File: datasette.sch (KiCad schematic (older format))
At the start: 30 parts, among them CN3 CASSETTE, CN7 SERIAL_BUS, Q5 2SD880, U11 74LS125, U9 74LS06

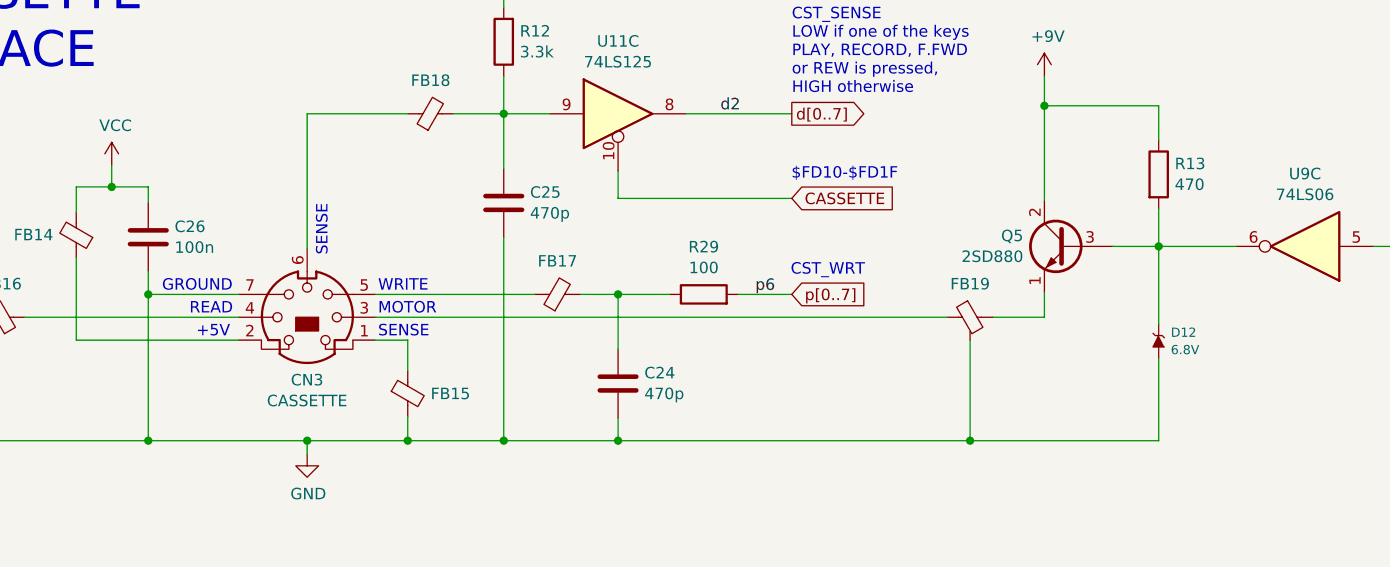
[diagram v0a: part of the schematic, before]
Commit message: Add support for PLA16V8
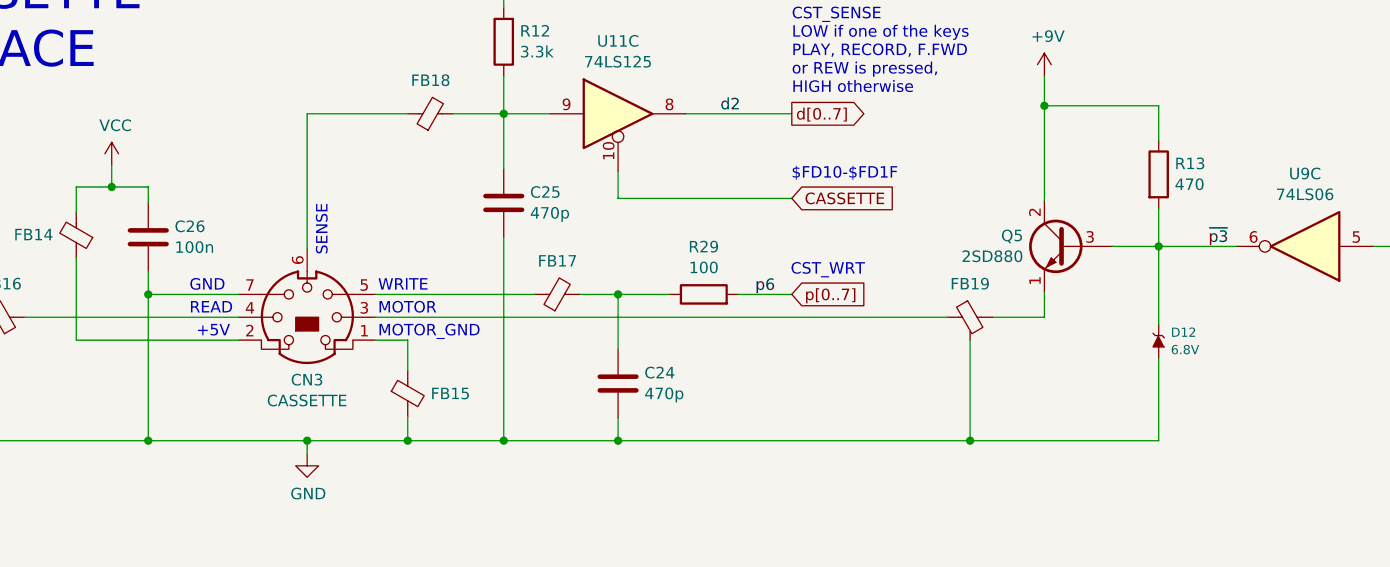
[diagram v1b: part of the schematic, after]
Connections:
- net ~p3: now reaches D12.2 (K), Q5.3 (B), R13.2, U9.6
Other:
- note added: "MOTOR_GND"
- note removed: "GROUND"
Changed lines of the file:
@@
 MOTOR
 Text Notes 5350 2560 0    50   ~ 0
-SENSE
-Text Notes 4405 2360 0    50   ~ 0
-GROUND
+MOTOR_GND
+Text Notes 4525 2360 0    50   ~ 0
+GND
 Text Notes 4525 2460 0    50   ~ 0
 READ
@@
 Wire Bus Line
 	3565 4640 3565 5520
+Text Label 9070 2155 2    50   ~ 0
+~p3
 $EndSCHEMATC

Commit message: Switch to Kycon MiniDIN connectors
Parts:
- removed CN3: CASSETTE, LittleSixteen:Connector_Mini-DIN_Female_7Pin_2rows, symbol Connector:Mini-DIN-7
- added CN3: CASSETTE, LittleSixteen:KMDGX-7S-BS, symbol mini-din-7:Mini-DIN-7
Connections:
- net GND: now also CN3.0 (SH), CN3.8
- net at FB19.1: now also CN3.3
- net at FB15.1: now also CN3.1
- net at FB14.1: now also CN3.2
- net at FB16.1: now also CN3.5
- net at FB17.1: now also CN3.6
- net at FB18.1: now also CN3.7
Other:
- note added: "WARNING: The drawing of\nthis connector does not\nmatch the real connector\nexactly!"
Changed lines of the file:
@@
 Sheet 7 12
 Title "LittleSixteen"
-Date "2021-10-31"
+Date "2021-11-06"
 Rev "2git"
 Comp "SukkoPera"
@@
 Comment4 ""
 $EndDescr
-$Comp
-L Connector:Mini-DIN-7 CN3
-U 1 1 5ECB4902
-P 5040 2465
-F 0 "CN3" H 5040 2190 50  0000 C CNN
-F 1 "CASSETTE" H 5040 2099 50  0000 C CNN
-F 2 "LittleSixteen:Connector_Mini-DIN_Female_7Pin_2rows" V 5030 2455 50  0001 C CNN
-F 3 "http://service.powerdynamics.com/ec/Catalog17/Section%2011.pdf" V 5030 2455 50  0001 C CNN
-	1    5040 2465
-	1    0    0    -1
-$EndComp
 Wire Wire Line
 	4740 2365 4345 2365
@@
 Text Notes 3495 4505 2    50   ~ 0
 These are more retrofitted\nprotection diodes, these\nare present on most C16s\nI've seen; note that these\ndiodes have been added on all\npins going straight to the CPU
+Text Label 9070 2155 2    50   ~ 0
+~p3
+$Comp
+L mini-din-7:Mini-DIN-7 CN3
+U 1 1 620EE6EF
+P 5040 2465
+F 0 "CN3" H 4845 2215 50  0000 C CNN
+F 1 "CASSETTE" H 4745 2130 50  0000 C CNN
+F 2 "LittleSixteen:KMDGX-7S-BS" V 5030 2455 50  0001 C CNN
+F 3 "http://service.powerdynamics.com/ec/Catalog17/Section%2011.pdf" V 5030 2455 50  0001 C CNN
+	1    5040 2465
+	1    0    0    -1
+$EndComp
+Text Notes 4995 2155 1    50   ~ 0
+WARNING: The drawing of\nthis connector does not\nmatch the real connector\nexactly!
+Wire Wire Line
+	5040 2765 5040 3005
 Wire Bus Line
 	3565 4640 3565 5520
-Text Label 9070 2155 2    50   ~ 0
-~p3
 $EndSCHEMATC

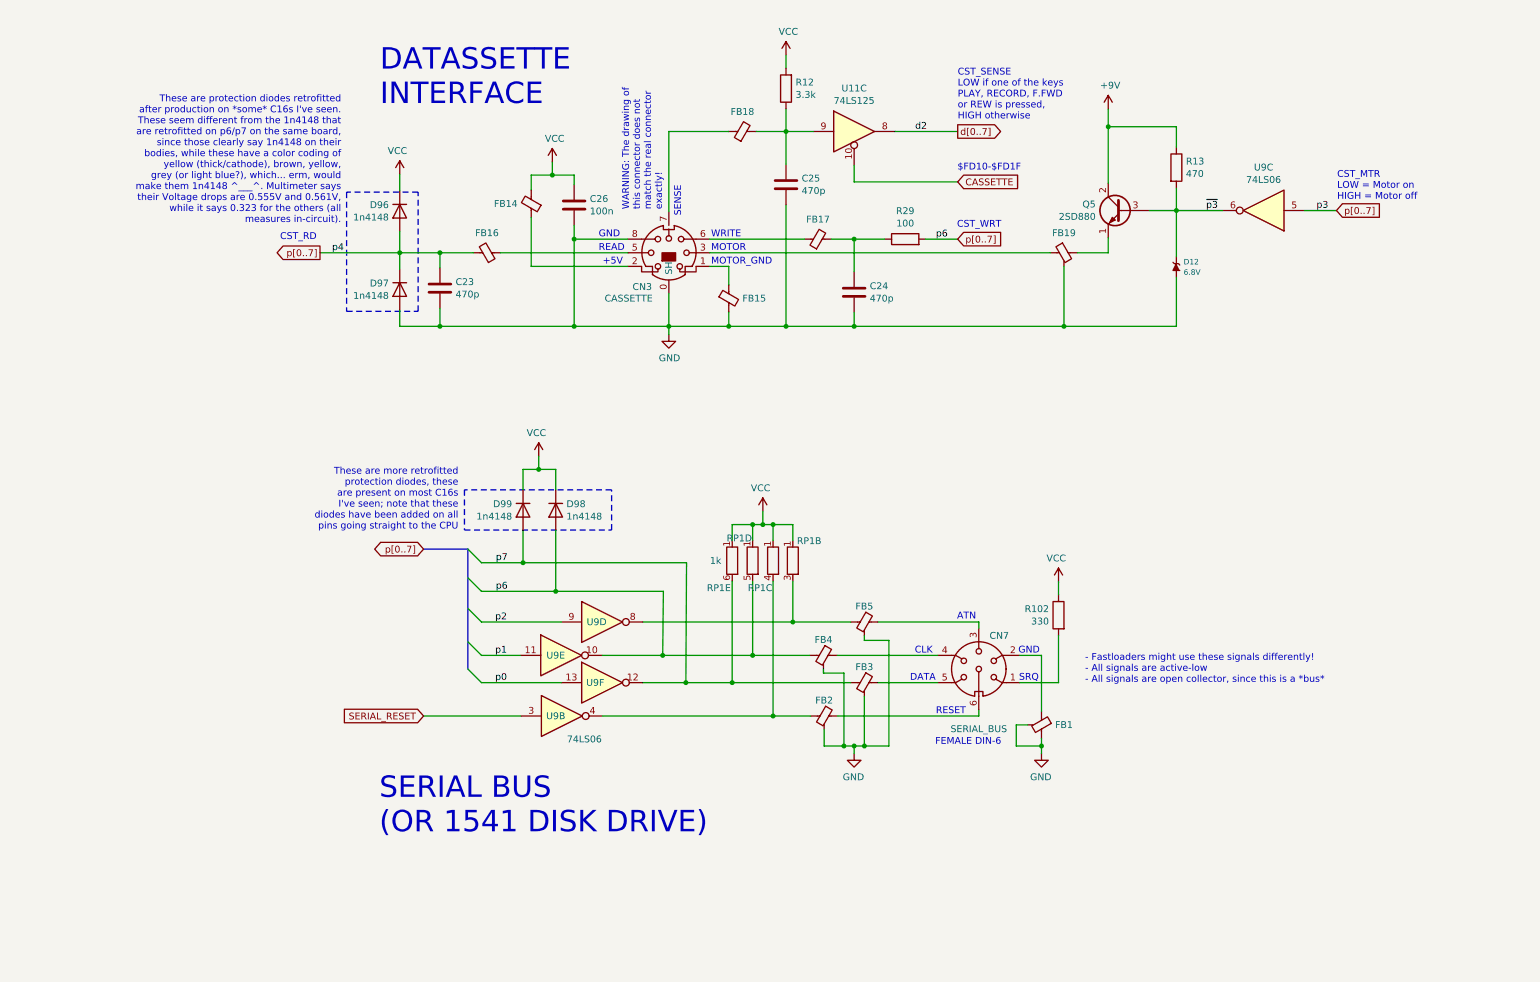
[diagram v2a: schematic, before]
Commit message: Add some protection diodes we'd overlooked
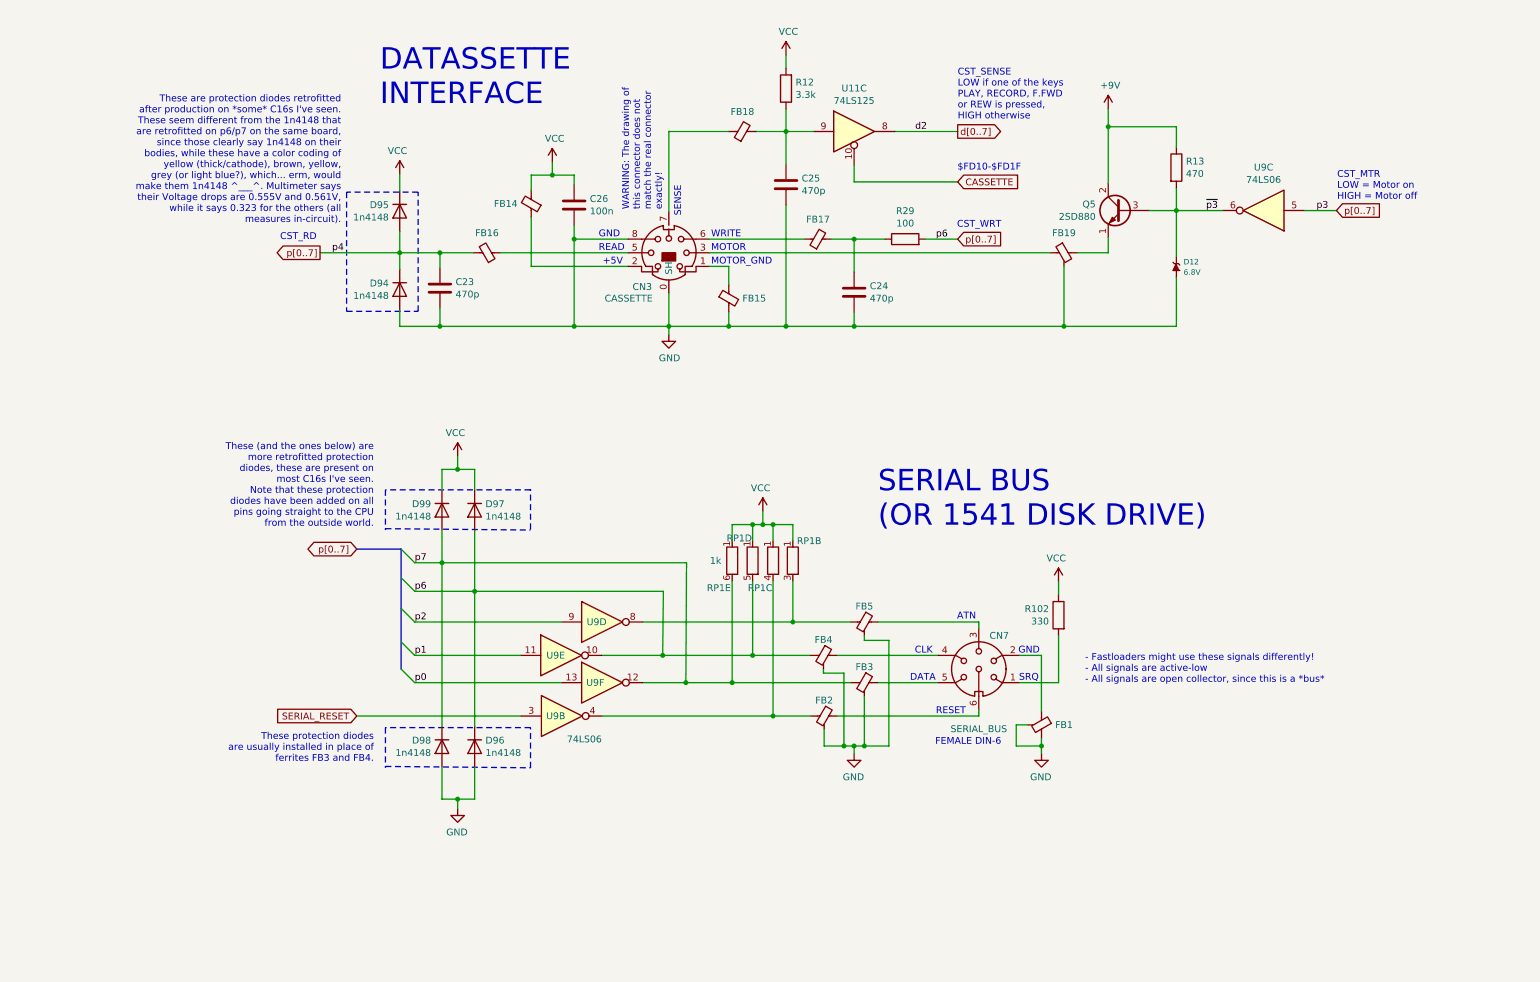
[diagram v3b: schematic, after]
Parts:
- added D96, D98: 1n4148, Diode_THT:D_DO-35_SOD27_P5.08mm_Vertical_KathodeUp, symbol Device:D
- renumbered D97 to D94, D96 to D95, D98 to D97
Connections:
- net GND: now also D96.2 (A), D98.2 (A)
- net p7: now also D98.1 (K)
- net p[0..7]: now also D96.1 (K)
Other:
- note added: "These (and the ones below) are\nmore retrofitted protection\ndiodes, these are present on\nmost C16s I've seen.\nNote that these protection\ndiodes have been added on all\npins going straight to the CPU\nfrom the outside world."
- note added: "These protection diodes\nare usually installed in place of\nferrites FB3 and FB4."
- note removed: "These are more retrofitted\nprotection diodes, these\nare present on most C16s\nI've seen; note that these\ndiodes have been added on all\npins going straight to the CPU"
- moved on the sheet: D97, D99
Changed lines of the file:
@@
 Sheet 7 12
 Title "LittleSixteen"
-Date "2021-11-06"
+Date "2021-11-17"
 Rev "2git"
 Comp "SukkoPera"
@@
 Wire Wire Line
 	6375 5175 5950 5175
-Text Label 3765 5175 0    50   ~ 0
+Text Label 3175 5175 0    50   ~ 0
 p2
 Wire Wire Line
 	6075 5420 5655 5420
 Wire Wire Line
-	3950 5420 3665 5420
-Text Label 3765 5420 0    50   ~ 0
+	3950 5420 3175 5420
+Text Label 3175 5420 0    50   ~ 0
 p1
 $Comp
@@
 $EndComp
 Wire Wire Line
-	4250 5620 3665 5620
-Text Label 3765 5620 0    50   ~ 0
+	4250 5620 3175 5620
+Text Label 3175 5620 0    50   ~ 0
 p0
 Wire Wire Line
-	4250 5175 3665 5175
+	4250 5175 3175 5175
 Wire Wire Line
 	7315 5865 6280 5865
@@
 Wire Wire Line
 	5505 5620 5165 5620
-Text GLabel 3240 4640 0    50   BiDi ~ 0
+Text GLabel 2750 4640 0    50   BiDi ~ 0
 p[0..7]
 Entry Wire Line
-	3665 5175 3565 5075
+	3175 5175 3075 5075
 Entry Wire Line
-	3665 5420 3565 5320
+	3175 5420 3075 5320
 Entry Wire Line
-	3665 5620 3565 5520
+	3175 5620 3075 5520
 Wire Wire Line
 	4995 5420 5000 4950
-Wire Wire Line
-	5000 4950 4210 4950
 Connection ~ 4995 5420
 Wire Wire Line
 	4995 5420 4550 5420
-Text Label 3770 4950 0    50   ~ 0
+Text Label 3175 4950 0    50   ~ 0
 p6
 Wire Wire Line
@@
 Wire Wire Line
 	5165 5620 4850 5620
-Text Label 3770 4740 0    50   ~ 0
+Text Label 3175 4740 0    50   ~ 0
 p7
 Entry Wire Line
-	3665 4950 3565 4850
+	3175 4950 3075 4850
 Entry Wire Line
-	3665 4740 3565 4640
+	3175 4740 3075 4640
 Wire Bus Line
-	3565 4640 3240 4640
-Text GLabel 3240 5865 0    50   Input ~ 0
+	3075 4640 2750 4640
+Text GLabel 2750 5865 0    50   Input ~ 0
 SERIAL_RESET
 Wire Wire Line
-	3955 5865 3240 5865
-Text Notes 2915 6740 0    157  ~ 0
+	3955 5865 2750 5865
+Text Notes 6575 4490 0    157  ~ 0
 SERIAL BUS\n(OR 1541 DISK DRIVE)
 Text Notes 2920 1395 0    157  ~ 0
@@
 	7940 3005 6400 3005
 $Comp
-L Device:D D98
+L Device:D D97
 U 1 1 61845FF9
-P 4210 4355
-F 0 "D98" V 4164 4276 50  0000 R CNN
-F 1 "1n4148" V 4255 4276 50  0000 R CNN
-F 2 "Diode_THT:D_DO-35_SOD27_P5.08mm_Vertical_KathodeUp" H 4210 4355 50  0001 C CNN
-F 3 "~" H 4210 4355 50  0001 C CNN
-	1    4210 4355
+P 3615 4355
+F 0 "D97" V 3569 4276 50  0000 R CNN
+F 1 "1n4148" V 3660 4276 50  0000 R CNN
+F 2 "Diode_THT:D_DO-35_SOD27_P5.08mm_Vertical_KathodeUp" H 3615 4355 50  0001 C CNN
+F 3 "~" H 3615 4355 50  0001 C CNN
+	1    3615 4355
 	0    -1   1    0
 $EndComp
 Wire Wire Line
-	4210 4505 4210 4950
-Connection ~ 4210 4950
-Wire Wire Line
-	4210 4950 3665 4950
-Wire Wire Line
-	4210 4205 4210 4055
+	3615 4505 3615 4950
+Wire Wire Line
+	3615 4205 3615 4055
 Text Notes 5135 1975 3    50   ~ 0
 SENSE
@@
 +5V
 Wire Notes Line
-	3540 4205 3540 4500
-Wire Notes Line
-	4620 4500 4620 4205
+	2960 4205 2960 4500
+Wire Notes Line
+	4025 4495 4025 4200
 Text Notes 2635 2255 2    50   ~ 0
 These are protection diodes retrofitted\nafter production on *some* C16s I've seen.\nThese seem different from the 1n4148 that\nare retrofitted on p6/p7 on the same board,\nsince those clearly say 1n4148 on their\nbodies, while these have a color coding of\nyellow (thick/cathode), brown, yellow,\ngrey (or light blue?), which... erm, would\nmake them 1n4148 ^___^. Multimeter says\ntheir Voltage drops are 0.555V and 0.561V,\nwhile it says 0.323 for the others (all\nmeasures in-circuit).
@@
 - Fastloaders might use these signals differently!\n- All signals are active-low\n- All signals are open collector, since this is a *bus*
 Connection ~ 3360 2465
-Connection ~ 3970 4740
-Wire Wire Line
-	3970 4740 3665 4740
-Wire Wire Line
-	5170 4740 3970 4740
-Wire Notes Line
-	3540 4500 4620 4500
-Wire Notes Line
-	4620 4205 3540 4205
-Wire Wire Line
-	4085 4055 3970 4055
-Connection ~ 4085 4055
-Wire Wire Line
-	4085 3960 4085 4055
+Wire Notes Line
+	2960 4490 4025 4500
+Wire Notes Line
+	4025 4205 2960 4205
+Wire Wire Line
+	3490 4055 3375 4055
+Connection ~ 3490 4055
+Wire Wire Line
+	3490 3960 3490 4055
 $Comp
 L power:VCC #PWR0191
 U 1 1 61857C18
-P 4085 3960
-F 0 "#PWR0191" H 4085 3810 50  0001 C CNN
-F 1 "VCC" H 4102 4133 50  0000 C CNN
-F 2 "" H 4085 3960 50  0001 C CNN
-F 3 "" H 4085 3960 50  0001 C CNN
-	1    4085 3960
-	-1   0    0    -1
-$EndComp
-Wire Wire Line
-	3970 4055 3970 4205
-Wire Wire Line
-	4210 4055 4085 4055
-Wire Wire Line
-	3970 4505 3970 4740
+P 3490 3960
+F 0 "#PWR0191" H 3490 3810 50  0001 C CNN
+F 1 "VCC" H 3507 4133 50  0000 C CNN
+F 2 "" H 3490 3960 50  0001 C CNN
+F 3 "" H 3490 3960 50  0001 C CNN
+	1    3490 3960
+	-1   0    0    -1
+$EndComp
+Wire Wire Line
+	3375 4055 3375 4205
+Wire Wire Line
+	3615 4055 3490 4055
+Wire Wire Line
+	3375 4505 3375 4740
 $Comp
 L Device:D D99
 U 1 1 61845668
-P 3970 4355
-F 0 "D99" V 3924 4435 50  0000 L CNN
-F 1 "1n4148" V 4015 4435 50  0000 L CNN
-F 2 "Diode_THT:D_DO-35_SOD27_P5.08mm_Vertical_KathodeUp" H 3970 4355 50  0001 C CNN
-F 3 "~" H 3970 4355 50  0001 C CNN
-	1    3970 4355
+P 3375 4355
+F 0 "D99" V 3329 4435 50  0000 L CNN
+F 1 "1n4148" V 3420 4435 50  0000 L CNN
+F 2 "Diode_THT:D_DO-35_SOD27_P5.08mm_Vertical_KathodeUp" H 3375 4355 50  0001 C CNN
+F 3 "~" H 3375 4355 50  0001 C CNN
+	1    3375 4355
 	0    -1   1    0
 $EndComp
@@
 	4345 3005 5040 3005
 $Comp
-L Device:D D96
+L Device:D D95
 U 1 1 619101DA
 P 3065 2160
-F 0 "D96" V 3019 2240 50  0000 L CNN
+F 0 "D95" V 3019 2240 50  0000 L CNN
 F 1 "1n4148" V 3110 2240 50  0000 L CNN
 F 2 "Diode_THT:D_DO-35_SOD27_P5.08mm_Vertical_KathodeUp" H 3065 2160 50  0001 C CNN
@@
 	3065 1890 3065 2010
 $Comp
-L Device:D D97
+L Device:D D94
 U 1 1 619101EB
 P 3065 2735
-F 0 "D97" V 3019 2815 50  0000 L CNN
+F 0 "D94" V 3019 2815 50  0000 L CNN
 F 1 "1n4148" V 3110 2815 50  0000 L CNN
 F 2 "Diode_THT:D_DO-35_SOD27_P5.08mm_Vertical_KathodeUp" H 3065 2735 50  0001 C CNN
@@
 Wire Notes Line
 	3200 2020 2675 2020
-Text Notes 3495 4505 2    50   ~ 0
-These are more retrofitted\nprotection diodes, these\nare present on most C16s\nI've seen; note that these\ndiodes have been added on all\npins going straight to the CPU
+Text Notes 2875 4485 2    50   ~ 0
+These (and the ones below) are\nmore retrofitted protection\ndiodes, these are present on\nmost C16s I've seen.\nNote that these protection\ndiodes have been added on all\npins going straight to the CPU\nfrom the outside world.
 Text Label 9070 2155 2    50   ~ 0
 ~p3
@@
 Wire Wire Line
 	5040 2765 5040 3005
+Connection ~ 3375 4740
+Wire Wire Line
+	3375 4740 3175 4740
+Connection ~ 3615 4950
+Wire Wire Line
+	3615 4950 3175 4950
+Wire Wire Line
+	3615 4950 5000 4950
+Wire Wire Line
+	3375 4740 5170 4740
+$Comp
+L Device:D D96
+U 1 1 6195D0A7
+P 3615 6090
+F 0 "D96" V 3569 6011 50  0000 R CNN
+F 1 "1n4148" V 3660 6011 50  0000 R CNN
+F 2 "Diode_THT:D_DO-35_SOD27_P5.08mm_Vertical_KathodeUp" H 3615 6090 50  0001 C CNN
+F 3 "~" H 3615 6090 50  0001 C CNN
+	1    3615 6090
+	0    -1   1    0
+$EndComp
+Wire Wire Line
+	3615 6240 3615 6475
+Wire Wire Line
+	3375 6240 3375 6475
+$Comp
+L Device:D D98
+U 1 1 6195D577
+P 3375 6090
+F 0 "D98" V 3329 6170 50  0000 L CNN
+F 1 "1n4148" V 3420 6170 50  0000 L CNN
+F 2 "Diode_THT:D_DO-35_SOD27_P5.08mm_Vertical_KathodeUp" H 3375 6090 50  0001 C CNN
+F 3 "~" H 3375 6090 50  0001 C CNN
+	1    3375 6090
+	0    -1   1    0
+$EndComp
+Wire Wire Line
+	3375 4740 3375 5940
+Wire Wire Line
+	3615 4950 3615 5940
+Wire Wire Line
+	3375 6475 3490 6475
+Wire Wire Line
+	3490 6475 3490 6545
+Connection ~ 3490 6475
+Wire Wire Line
+	3490 6475 3615 6475
+$Comp
+L power:GND #PWR0207
+U 1 1 6198FDCB
+P 3490 6545
+F 0 "#PWR0207" H 3490 6295 50  0001 C CNN
+F 1 "GND" H 3495 6372 50  0000 C CNN
+F 2 "" H 3490 6545 50  0001 C CNN
+F 3 "" H 3490 6545 50  0001 C CNN
+	1    3490 6545
+	-1   0    0    -1
+$EndComp
+Wire Notes Line
+	2960 5950 2960 6245
+Wire Notes Line
+	2960 6235 4025 6245
+Wire Notes Line
+	4025 5950 2960 5950
+Wire Notes Line
+	4025 6245 4025 5950
 Wire Bus Line
-	3565 4640 3565 5520
+	3075 4640 3075 5520
+Text Notes 2875 6210 2    50   ~ 0
+These protection diodes\nare usually installed in place of\nferrites FB3 and FB4.
 $EndSCHEMATC
